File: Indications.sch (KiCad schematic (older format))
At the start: 32 parts

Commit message: updates
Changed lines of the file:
@@
-$EndComp
-$Comp
-L power:+5V #PWR?
-U 1 1 60F16AD2
-P 7400 2300
-AR Path="/60F16AD2" Ref="#PWR?"  Part="1"
-AR Path="/60EBA1DA/60F16AD2" Ref="#PWR?"  Part="1"
-F 0 "#PWR?" H 7400 2150 50  0001 C CNN
-F 1 "+5V" V 7415 2428 50  0000 L CNN
-F 2 "" H 7400 2300 50  0001 C CNN
-F 3 "" H 7400 2300 50  0001 C CNN
-	1    7400 2300
-	1    0    0    -1
 $EndComp
 $Comp
@@
 F 3 "" H 8150 3950 50  0001 C CNN
 	1    8150 3950
-	0    -1   -1   0
+	1    0    0    -1
 $EndComp
 Wire Wire Line
@@
 $EndComp
 Wire Wire Line
-	7400 2300 7400 2450
-Wire Wire Line
 	7400 2450 7400 3550
 Wire Wire Line
 	7400 3550 7650 3550
-Connection ~ 7400 2450
 Wire Wire Line
 	7650 3650 7350 3650
@@
 Text Notes 3650 4950 0    50   ~ 0
 Outboard Connector
+$Comp
+L power:+5V #PWR?
+U 1 1 60F16AD2
+P 7650 3550
+AR Path="/60F16AD2" Ref="#PWR?"  Part="1"
+AR Path="/60EBA1DA/60F16AD2" Ref="#PWR?"  Part="1"
+F 0 "#PWR?" H 7650 3400 50  0001 C CNN
+F 1 "+5V" V 7665 3678 50  0000 L CNN
+F 2 "" H 7650 3550 50  0001 C CNN
+F 3 "" H 7650 3550 50  0001 C CNN
+	1    7650 3550
+	1    0    0    -1
+$EndComp
+Connection ~ 7650 3550
 $EndSCHEMATC

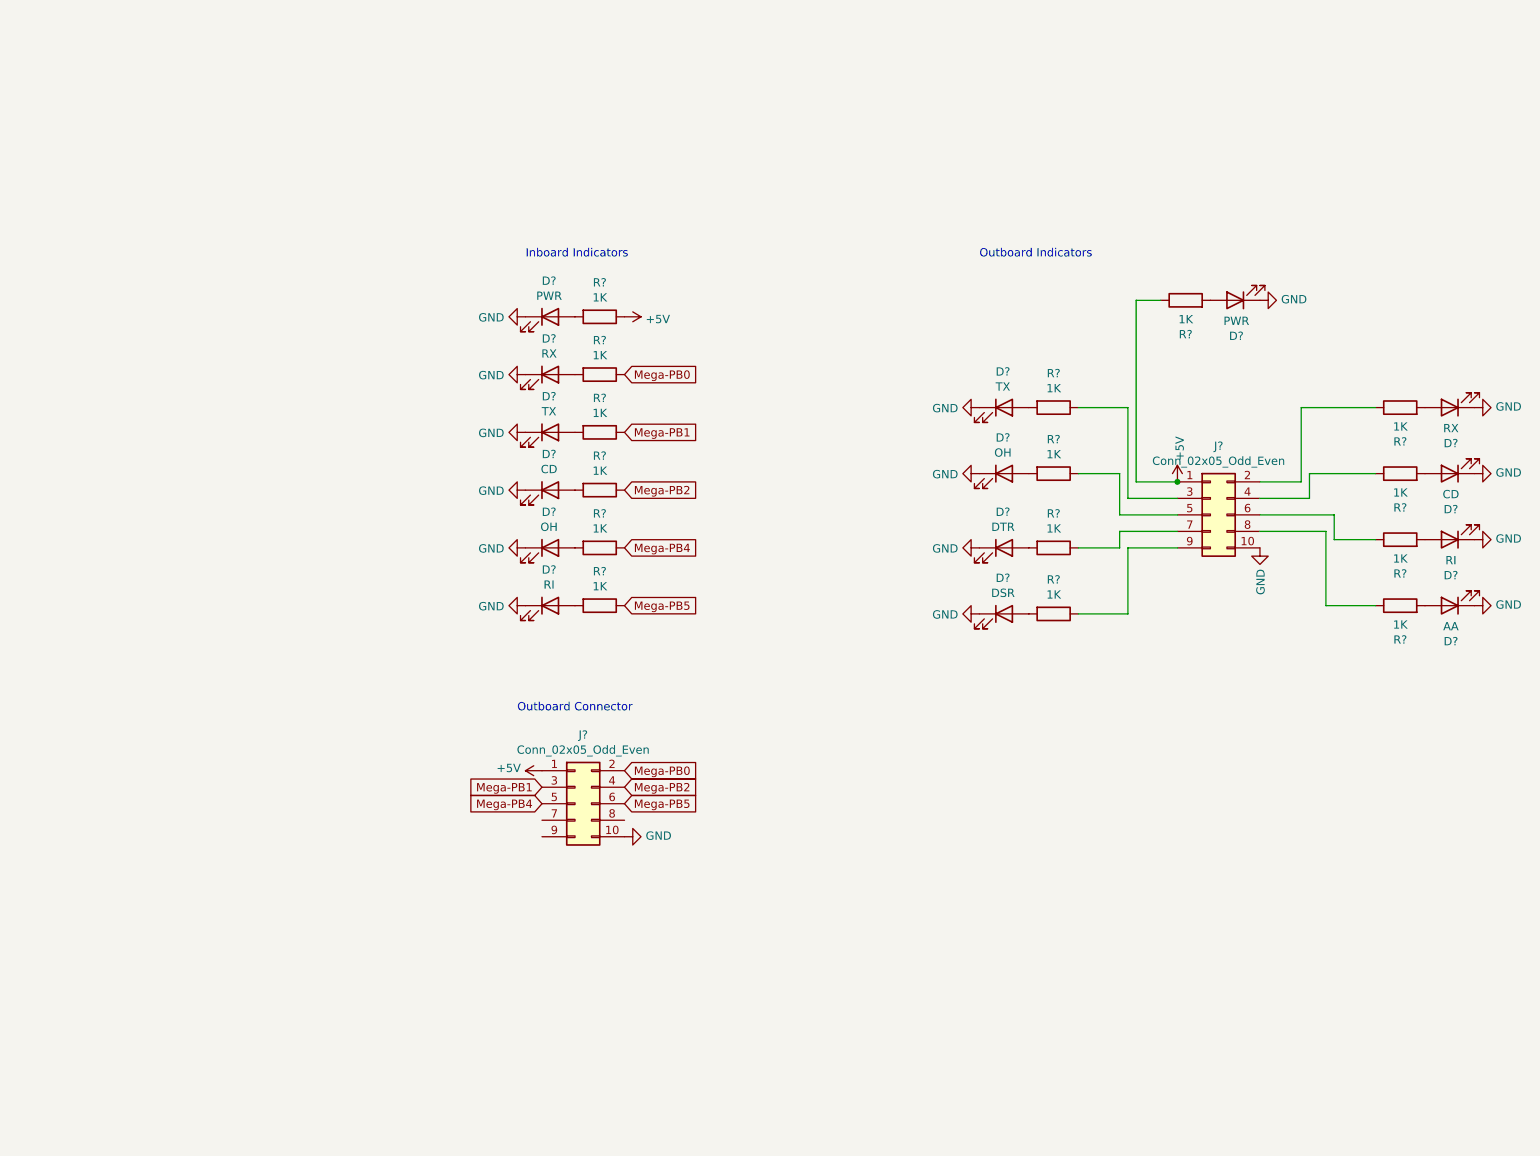
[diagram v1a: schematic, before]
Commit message: update to LEDs drive by NPN
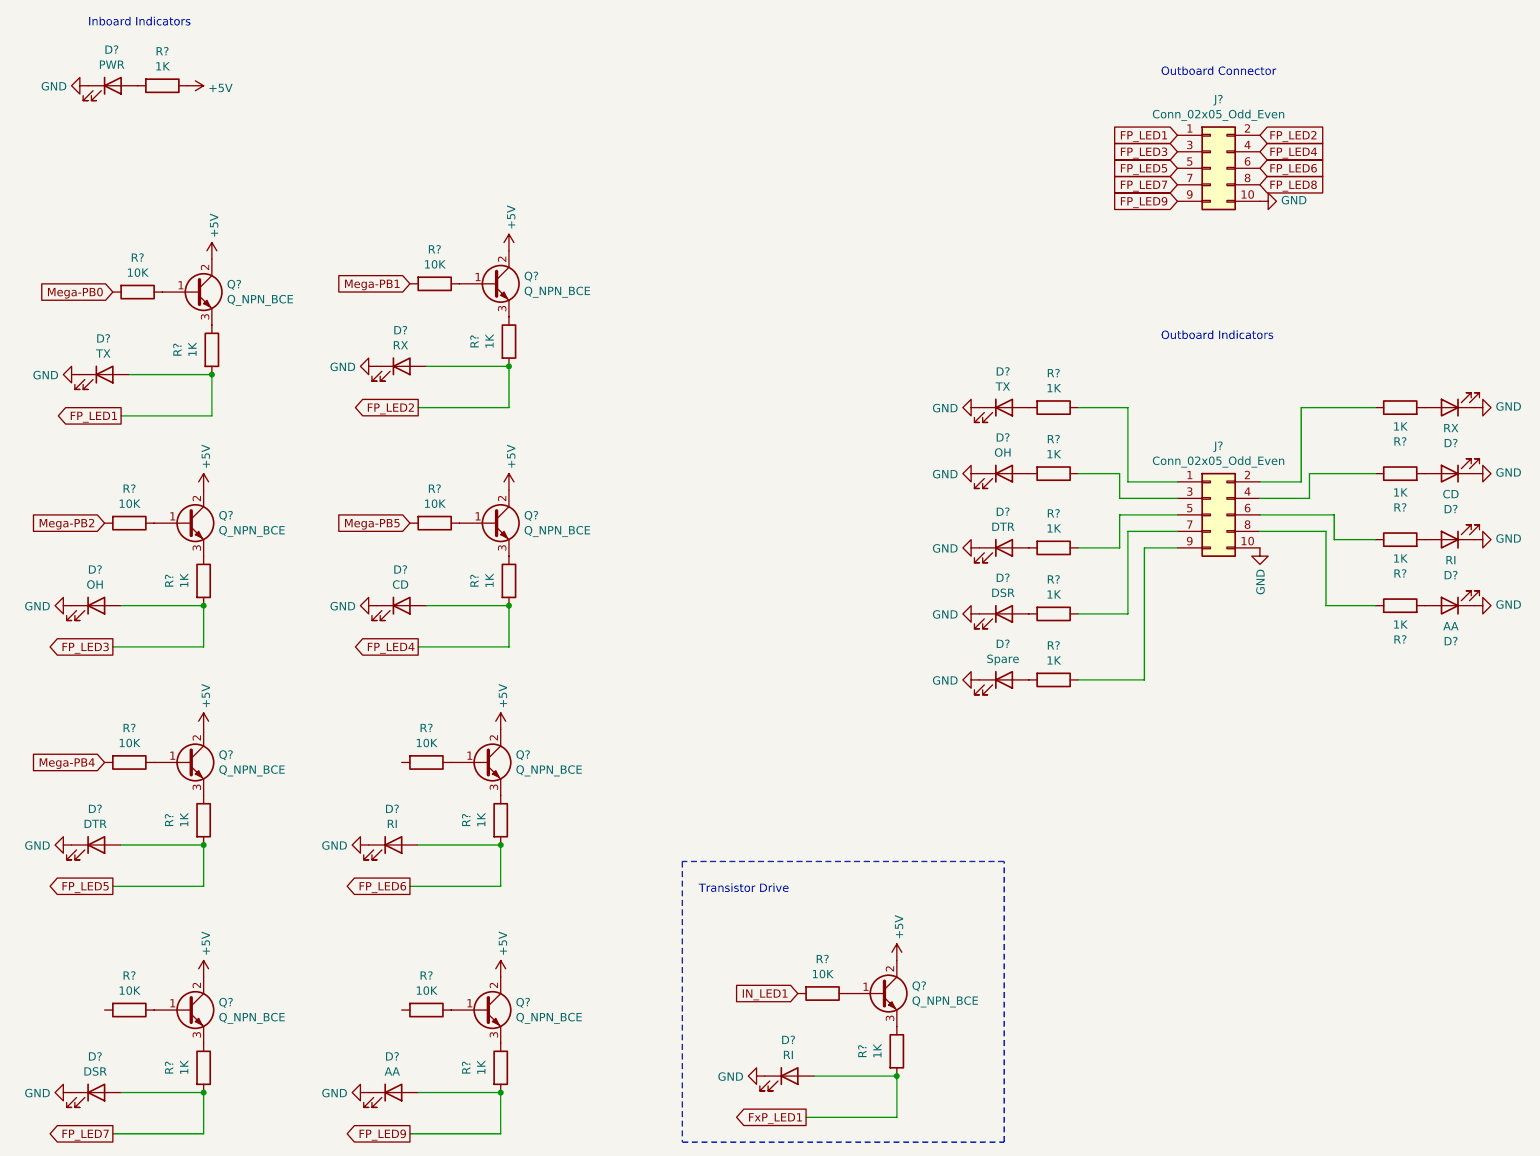
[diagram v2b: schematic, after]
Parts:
- removed D?: RX, symbol Device:LED
- removed D?: TX, symbol Device:LED
- removed D?: CD, symbol Device:LED
- removed D?: OH, symbol Device:LED
- removed D?: RI, symbol Device:LED
- removed D?: PWR, symbol Device:LED
- removed J?: Conn_02x05_Odd_Even, symbol Connector_Generic:Conn_02x05_Odd_Even
- removed R? (x6): 1K, symbol Device:R
- added D? (x2): RI, symbol Device:LED
- added D?: CD, symbol Device:LED
- added D?: TX, symbol Device:LED
- added D?: RX, symbol Device:LED
- added D?: OH, symbol Device:LED
- added D?: DTR, symbol Device:LED
- added D?: DSR, symbol Device:LED
- added D?: AA, symbol Device:LED
- added D?: Spare, symbol Device:LED
- added J?: Conn_02x05_Odd_Even, symbol Connector_Generic:Conn_02x05_Odd_Even
- added Q? (x9): Q_NPN_BCE, symbol Device:Q_NPN_BCE
- added R? (x9): 10K, symbol Device:R
- added R? (x10): 1K, symbol Device:R
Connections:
- net +5V: now also Q?.2 (C), Q?.2 (C), Q?.2 (C), Q?.2 (C), Q?.2 (C), Q?.2 (C), Q?.2 (C), Q?.2 (C), Q?.2 (C); no longer J?.1 (Pin_1)
- net GND: now also D?.1 (K), D?.1 (K), D?.1 (K), D?.1 (K), D?.1 (K), D?.1 (K), D?.1 (K), D?.1 (K), D?.1 (K), D?.1 (K), J?.10 (Pin_10)
- net Mega-PB0: now also R?.2
- net Mega-PB1: now also R?.2
- net Mega-PB2: now also R?.2
- net Mega-PB4: now also R?.2
- net Mega-PB5: now also R?.2
- net at R?.1: now also J?.3 (Pin_3); no longer J?.5 (Pin_5)
- net at R?.1: now also J?.1 (Pin_1); no longer J?.3 (Pin_3)
- net at R?.1: now also J?.5 (Pin_5); no longer J?.7 (Pin_7)
- net at R?.1: now also J?.7 (Pin_7); no longer J?.9 (Pin_9)
- new net: Q?.1 (B), R?.1 (x9)
- new net: Q?.3 (E), R?.1 (x9)
- new net: J?.9 (Pin_9), R?.1
- new net: D?.2 (A), R?.2
- new net FP_LED1: D?.2 (A), J?.1 (Pin_1), R?.2
- new net FP_LED2: D?.2 (A), J?.2 (Pin_2), R?.2
- new net FP_LED3: D?.2 (A), J?.3 (Pin_3), R?.2
- new net FP_LED4: D?.2 (A), J?.4 (Pin_4), R?.2
- new net FP_LED5: D?.2 (A), J?.5 (Pin_5), R?.2
- new net FP_LED6: D?.2 (A), J?.6 (Pin_6), R?.2
- new net FP_LED7: D?.2 (A), J?.7 (Pin_7), R?.2
- new net FP_LED8: J?.8 (Pin_8)
- new net FP_LED9: D?.2 (A), J?.9 (Pin_9), R?.2
- new net FxP_LED1: D?.2 (A), R?.2
- new net IN_LED1: R?.2
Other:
- note added: "Transistor Drive"
- moved on the sheet: D?, R?

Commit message: general updates
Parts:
- removed D?: RI, symbol Device:LED
- removed Q?: Q_NPN_BCE, symbol Device:Q_NPN_BCE
- removed R?: 10K, symbol Device:R
- removed R?: 1K, symbol Device:R
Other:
- note added: "To Outboard Connector"
- note removed: "Outboard Connector"
- note removed: "Transistor Drive"
- moved on the sheet: D?, Q?, R?

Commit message: sch updates
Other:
- moved on the sheet: D?, R?
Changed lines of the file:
@@
 L Device:R R?
 U 1 1 60EBEBFC
-P 3800 1450
+P 2750 1500
 AR Path="/60EBEBFC" Ref="R?"  Part="1"
 AR Path="/60EBA1DA/60EBEBFC" Ref="R?"  Part="1"
-F 0 "R?" V 3593 1450 50  0000 C CNN
-F 1 "1K" V 3684 1450 50  0000 C CNN
-F 2 "" V 3730 1450 50  0001 C CNN
-F 3 "~" H 3800 1450 50  0001 C CNN
-	1    3800 1450
+F 0 "R?" V 2543 1500 50  0000 C CNN
+F 1 "1K" V 2634 1500 50  0000 C CNN
+F 2 "" V 2680 1500 50  0001 C CNN
+F 3 "~" H 2750 1500 50  0001 C CNN
+	1    2750 1500
 	0    1    1    0
 $EndComp
@@
 L Device:LED D?
 U 1 1 60EBEC02
-P 3500 1450
+P 2450 1500
 AR Path="/60EBEC02" Ref="D?"  Part="1"
 AR Path="/60EBA1DA/60EBEC02" Ref="D?"  Part="1"
-F 0 "D?" H 3493 1667 50  0000 C CNN
-F 1 "PWR" H 3493 1576 50  0000 C CNN
-F 2 "" H 3500 1450 50  0001 C CNN
-F 3 "~" H 3500 1450 50  0001 C CNN
-	1    3500 1450
+F 0 "D?" H 2443 1717 50  0000 C CNN
+F 1 "PWR" H 2443 1626 50  0000 C CNN
+F 2 "" H 2450 1500 50  0001 C CNN
+F 3 "~" H 2450 1500 50  0001 C CNN
+	1    2450 1500
 	1    0    0    -1
 $EndComp
@@
 L power:GND #PWR?
 U 1 1 60EBEC08
-P 3350 1450
+P 2300 1500
 AR Path="/60EBEC08" Ref="#PWR?"  Part="1"
 AR Path="/60EBA1DA/60EBEC08" Ref="#PWR?"  Part="1"
-F 0 "#PWR?" H 3350 1200 50  0001 C CNN
-F 1 "GND" V 3355 1322 50  0000 R CNN
-F 2 "" H 3350 1450 50  0001 C CNN
-F 3 "" H 3350 1450 50  0001 C CNN
-	1    3350 1450
+F 0 "#PWR?" H 2300 1250 50  0001 C CNN
+F 1 "GND" V 2305 1372 50  0000 R CNN
+F 2 "" H 2300 1500 50  0001 C CNN
+F 3 "" H 2300 1500 50  0001 C CNN
+	1    2300 1500
 	0    1    1    0
 $EndComp
@@
 L power:+5V #PWR?
 U 1 1 60EFA72E
-P 3950 1200
+P 2900 1250
 AR Path="/60EFA72E" Ref="#PWR?"  Part="1"
 AR Path="/60EBA1DA/60EFA72E" Ref="#PWR?"  Part="1"
-F 0 "#PWR?" H 3950 1050 50  0001 C CNN
-F 1 "+5V" V 3965 1328 50  0000 L CNN
-F 2 "" H 3950 1200 50  0001 C CNN
-F 3 "" H 3950 1200 50  0001 C CNN
-	1    3950 1200
-	1    0    0    -1
-$EndComp
-Text Notes 3200 800  0    50   ~ 0
+F 0 "#PWR?" H 2900 1100 50  0001 C CNN
+F 1 "+5V" V 2915 1378 50  0000 L CNN
+F 2 "" H 2900 1250 50  0001 C CNN
+F 3 "" H 2900 1250 50  0001 C CNN
+	1    2900 1250
+	1    0    0    -1
+$EndComp
+Text Notes 2150 850  0    50   ~ 0
 Inboard Indicators
 Text Notes 7550 2700 0    50   ~ 0
@@
 	7450 3950 7650 3950
 Wire Wire Line
-	3950 1450 3950 1200
+	2900 1500 2900 1250
 $EndSCHEMATC
